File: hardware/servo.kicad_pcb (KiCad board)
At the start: 2 copper layers, 43 x 44 mm, 40 parts, among them J1 5.5x2.1, J2 servo, J3 swd, J4 LED, Q1 DMT64M8LSS, SW1 restart, SW2 buzzer, U1 AOZ1284PI, U2 LDI1117-3.3U-DIO, U3 STM32G030F6Px

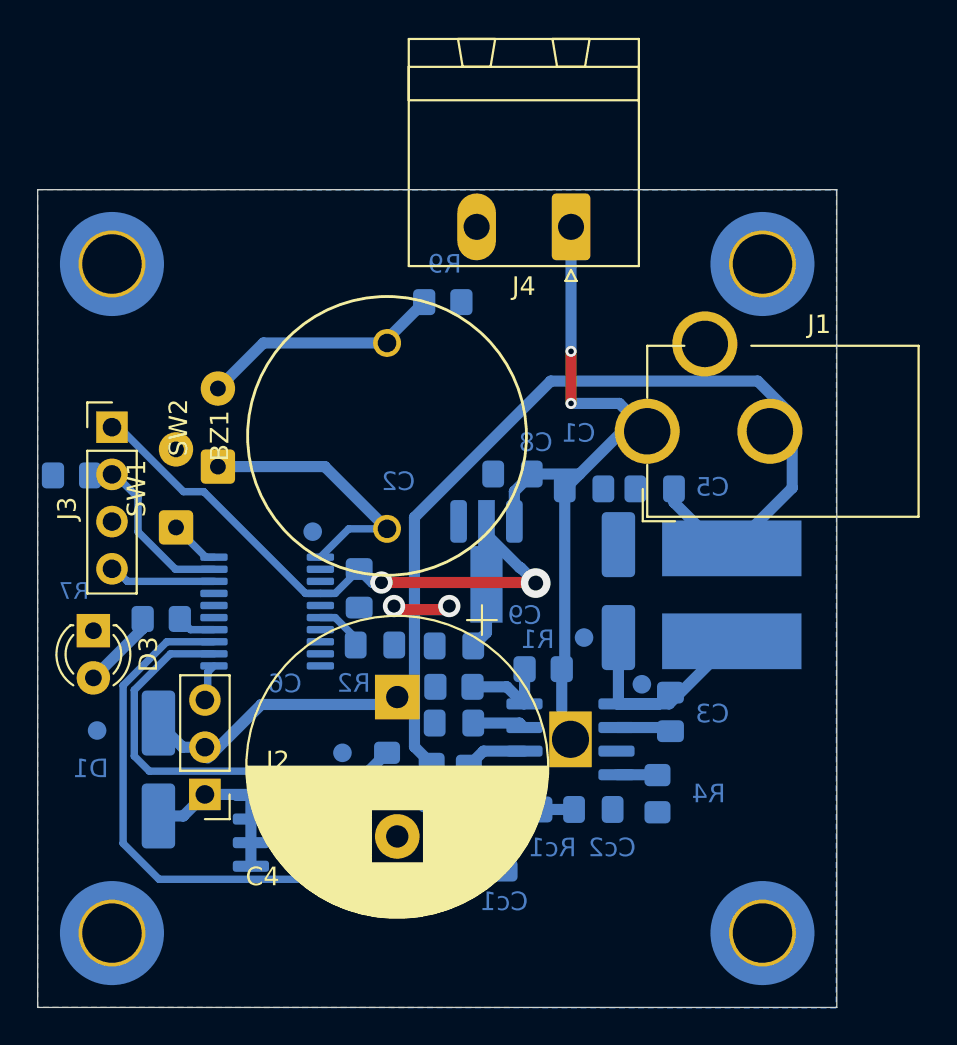
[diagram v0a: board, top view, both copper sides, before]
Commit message: Fix false stall detection after restart
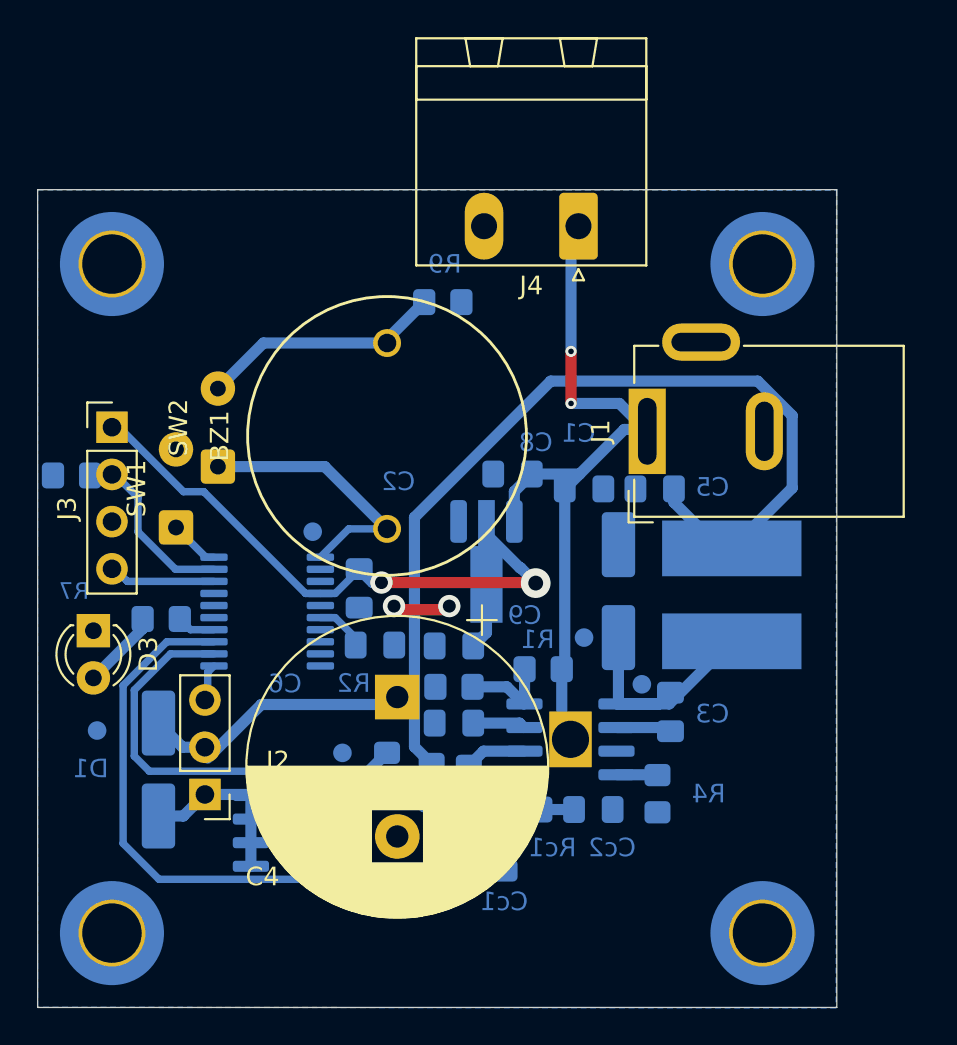
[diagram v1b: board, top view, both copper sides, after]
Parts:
- J1: footprint Connector_BarrelJack:BarrelJack_diy -> Connector_BarrelJack:BarrelJack_GCT_DCJ200-10-A_Horizontal
- moved J4 0.40 mm to (29.1, 1.96)
